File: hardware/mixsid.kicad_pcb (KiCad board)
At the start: 2 copper layers, 50.8 x 55.9 mm, 67 parts, among them P1 INPUT, P2 CONTROL, P4 SOCKET LEFT, P5 OUTPUT, P6 SOCKET RIGHT, Q1 BC547, Q2 BC547, U1 GAL16V8, U2 SID2, U3 7812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

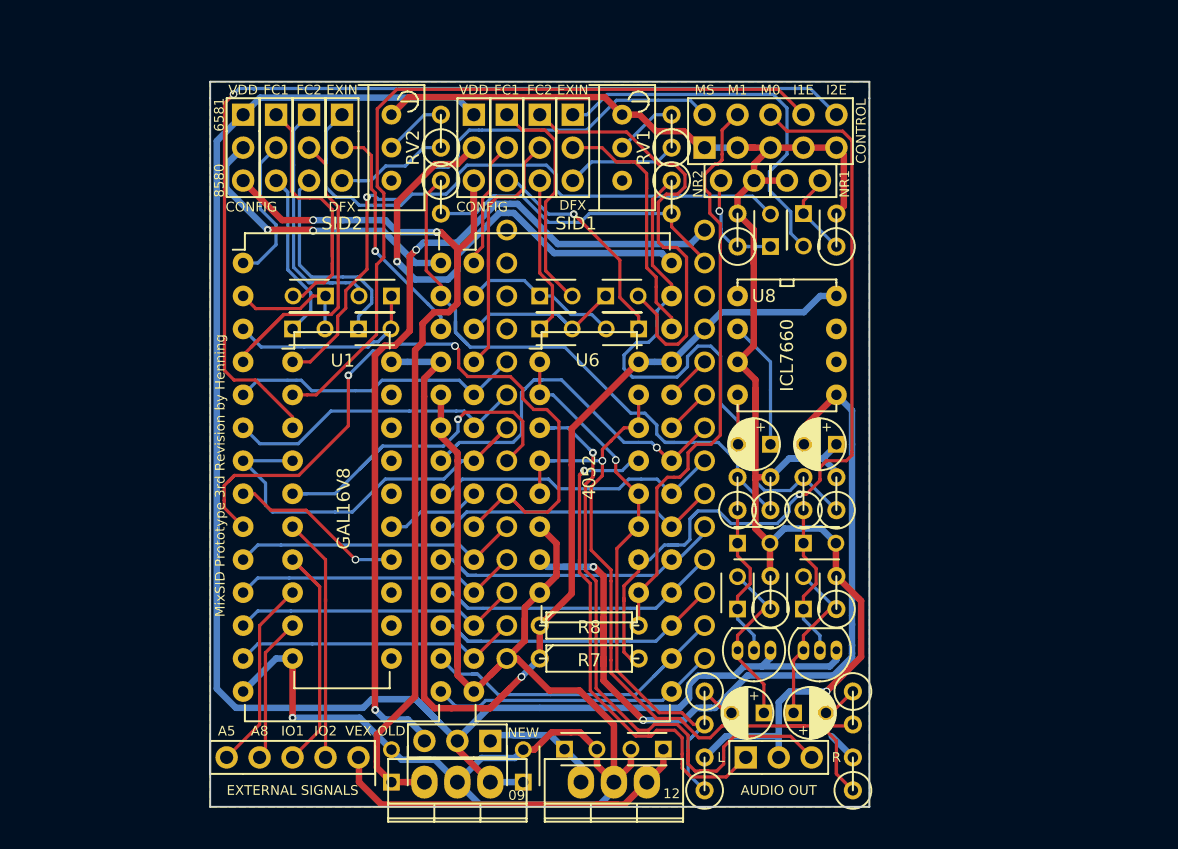
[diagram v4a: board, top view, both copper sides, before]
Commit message: Hardware: Priority, paddle multiplexing, volume adjust, bigger board size
Priority select has been reimplemented, allowing to virtually swap sids in
terms of addressing (which SID stays at home and which one goes stereo).

A 4053 multiplexer has been added to keep the paddles working regardless of
priority. Paddle lines are always routed to the SID currently at $d400.

Two pots have been added to allow volume adjustments before mixing in order
to adjust two different models in overall volume (6581 are usually louder).
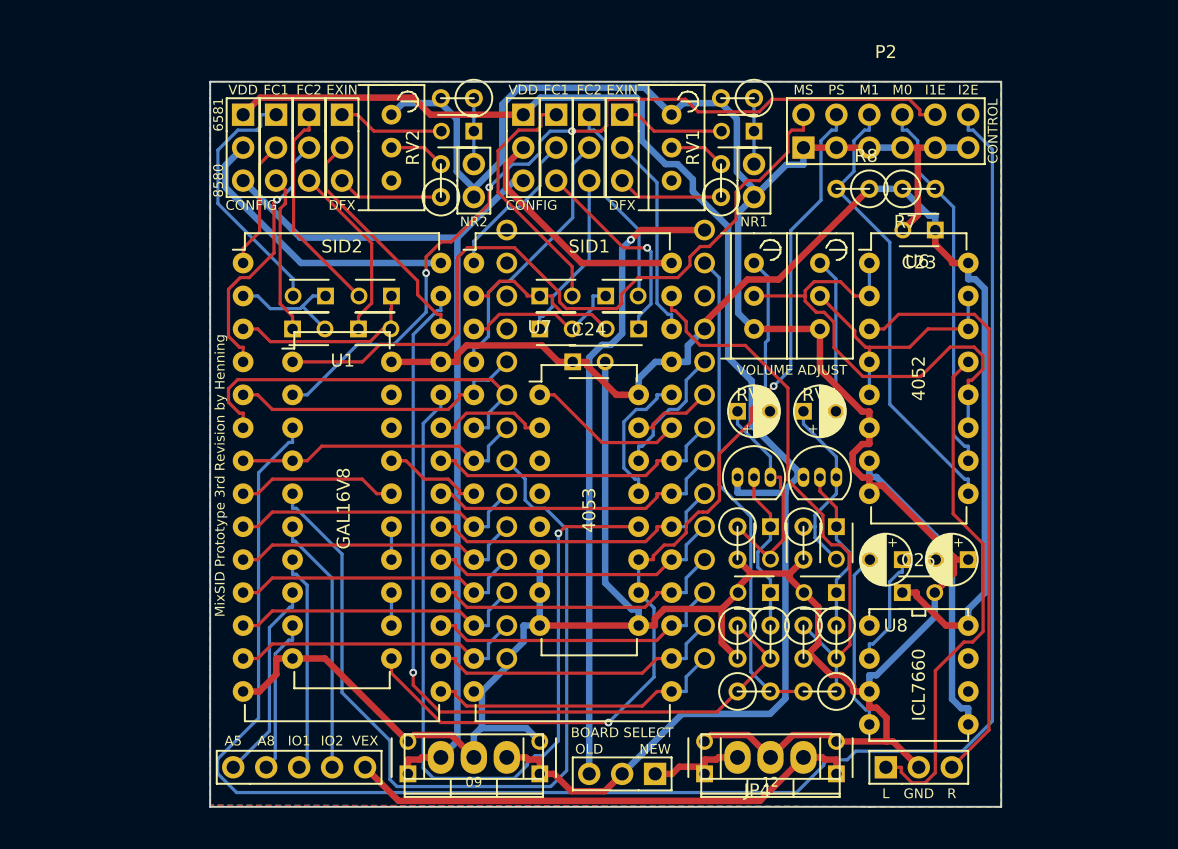
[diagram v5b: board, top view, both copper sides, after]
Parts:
- removed R15, R17: 0, Discret:R1
- removed R16, R18: ∞, Discret:R1
- added C23: 100n, Capacitors_ThroughHole:C_Disc_D3_P2.5, F.Cu at (184.2, 78.7)
- added C24: 100n, Capacitors_ThroughHole:C_Disc_D3_P2.5, F.Cu at (156.2, 88.9)
- added C25: 100n, Capacitors_ThroughHole:C_Disc_D3_P2.5, F.Cu at (181.6, 106.7)
- added RV3: 10k, Potentiometers:Potentiometer_Bourns_3296W_3-8Zoll_Inline_ScrewUp, F.Cu at (170.2, 81.3)
- added RV4: 10k, Potentiometers:Potentiometer_Bourns_3296W_3-8Zoll_Inline_ScrewUp, F.Cu at (175.3, 81.3)
- added U7: 4053, Housings_DIP:DIP-16_W7.62mm, F.Cu at (153.7, 91.4)
- P2: footprint Pinheaders:Pin_Header_Straight_2x05 -> Pinheaders:Pin_Header_Straight_2x06
- R7, R8: footprint Discret:R3 -> Discret:R1
- moved R13 45.1 mm to (170.2, 114.3), turned to 0 degrees
- moved R7 44.2 mm to (182.9, 75.6)
- moved R14 39.8 mm to (175.3, 114.3), turned to 180 degrees
- moved R8 39.3 mm to (177.8, 75.6), turned to 180 degrees
- moved U8 27.4 mm to (179.1, 109.2)
- moved U6 26.5 mm to (179.1, 81.3)
- moved C13 24.5 mm to (148.6, 71.1), turned to 180 degrees
- moved R9 23.9 mm to (147.3, 68.6), turned to 180 degrees
- moved C19 23.3 mm to (168.9, 92.7), turned to 0 degrees
- moved C22 23.3 mm to (174.0, 92.7)
- moved JP10 19.1 mm to (148.6, 73.7), turned to 0 degrees
- moved Q1 13.6 mm to (168.9, 97.8), turned to 0 degrees
- moved Q2 13.6 mm to (174.0, 97.8), turned to 0 degrees
- moved C17 13.5 mm to (181.6, 104.1)
- moved C18 13.5 mm to (186.7, 104.1)
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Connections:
- P2 pad 10: /~IO2EN -> /~IO1EN
- P2 pad 4: /M1 -> /PS
- P2 pad 6: /M0 -> /M1
- P2 pad 8: /~IO1EN -> /M0
- U1 pad 11: Net-(U1-Pad11) -> /PS
- U1 pad 13: Net-(U1-Pad13) -> Net-(U1-Pad12)
- U1 pad 14: /~CS2 -> Net-(U1-Pad14)
- U1 pad 15: /~CS1 -> Net-(U1-Pad14)
- U1 pad 16: Net-(U1-Pad16) -> /~CS2
- U1 pad 17: Net-(U1-Pad17) -> /~CS1
- U2 pad 23: GND -> /POTY2
- U2 pad 24: GND -> /POTX2
- U5 pad 23: /POTY -> /POTY1
- U5 pad 24: /POTX -> /POTX1
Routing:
- net /PS: track 0.00 -> 76.3 mm, vias 0 -> 2
- net /POTX2: track 0.00 -> 63.9 mm, vias 0 -> 1
- net /~IO2EN: track 76.7 -> 139.6 mm, vias 1 -> 0
- net /RIGHT: track 63.1 -> 20.1 mm, vias 1 -> 0
- net /VEE: track 66.3 -> 24.1 mm, vias 2 -> 0
- net Net-(C13-Pad2): track 46.3 -> 8.19 mm
- net /~CS: track 28.4 -> 66.0 mm, vias 1 -> 0
- net /M0: track 64.3 -> 29.2 mm, vias 1 -> 0
- net /A0: track 57.8 -> 23.0 mm, vias 2 -> 0
- net Net-(C14-Pad2): track 29.9 -> 8.19 mm
- net /PWR1: track 38.3 -> 18.8 mm, vias 1 -> 0
- net Net-(C9-Pad2): track 34.9 -> 15.8 mm
- net VDD: track 67.7 -> 48.9 mm, vias 2 -> 1
- net /S2OUT: track 48.1 -> 64.8 mm, vias 0 -> 1
- net /MONO_OUT: track 24.3 -> 37.7 mm
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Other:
- board size 50.8 x 55.9 mm -> 61 x 55.9 mm
- board text added: "BOARD SELECT"
- board text added: "GND"
- board text added: "PS"
- board text added: "VOLUME ADJUST"
- board text removed: "AUDIO OUT"
- board text removed: "EXTERNAL SIGNALS"

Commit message: Hardware: Replaced balance pots with round types (bourns 3339), rearranged
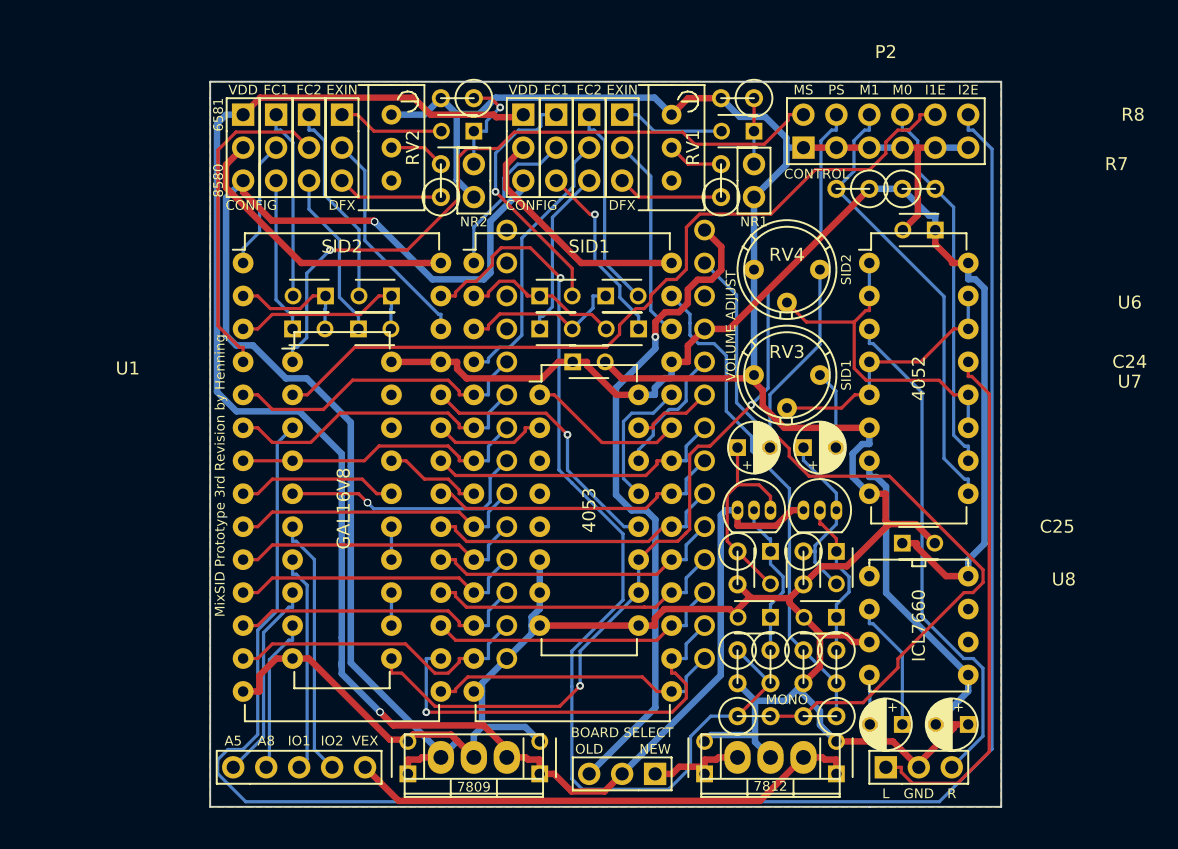
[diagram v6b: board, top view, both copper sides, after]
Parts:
- RV3, RV4: footprint Potentiometers:Potentiometer_Bourns_3296W_3-8Zoll_Inline_ScrewUp -> Potentiometers:Potentiometer_Bourns_3339P_Angular_ScrewUp
- moved C17 12.7 mm to (181.6, 116.8)
- moved C18 12.7 mm to (186.7, 116.8)
- moved RV4 8.64 mm to (175.3, 89.9)
- moved RV3 5.11 mm to (175.3, 81.8)
- moved C25 3.81 mm to (181.6, 102.9)
- moved U8 3.81 mm to (179.1, 105.4)
- moved C19 2.79 mm to (168.9, 95.5)
- moved C22 2.79 mm to (174.0, 95.5)
- moved Q1 2.54 mm to (168.9, 100.3)
- moved Q2 2.54 mm to (174.0, 100.3)
- moved C16 1.91 mm to (171.4, 103.5)
- moved C21 1.91 mm to (176.5, 103.5)
- moved R11 1.91 mm to (176.5, 112.4)
- moved R12 1.91 mm to (174.0, 104.8)
- moved R13 1.91 mm to (170.2, 116.2)
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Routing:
- net /~CS: track 66.0 -> 19.6 mm, vias 0 -> 1
- net /POTX2: track 63.9 -> 21.0 mm
- net /MONO_OUT: track 37.7 -> 58.5 mm, vias 0 -> 1
- net /+9V: track 69.5 -> 90.2 mm, vias 0 -> 1
- net GND: track 264.1 -> 243.7 mm
- net /+12V: track 115.8 -> 132.9 mm, vias 0 -> 1
- net /S2OUT: track 64.8 -> 78.6 mm
- net /LEFT: track 37.6 -> 26.7 mm
- net /D1: track 23.1 -> 33.7 mm, vias 0 -> 1
- net Net-(C17-Pad2): track 13.8 -> 3.83 mm
- net /RIGHT_OUT: track 45.1 -> 39.0 mm
- net /CLK: track 30.1 -> 24.1 mm
- net Net-(C22-Pad2): track 11.9 -> 6.10 mm
- net Net-(JP2-Pad2): track 20.2 -> 25.4 mm, vias 1 -> 0
- net Net-(C3-Pad2): track 19.8 -> 14.7 mm
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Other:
- board text added: "7809"
- board text added: "7812"
- board text added: "MONO"
- board text added: "SID1"
- board text added: "SID2"
- board text removed: "09"
- board text removed: "12"

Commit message: Firmware/Hardware: RW2 signal controls SID2 RW during parallel addressing
Depending on RW2, SID2 is write-only or read-write when addressed alongside
SID1.

The default setting is write-only to assure proper paddle support.
For mono tunes that use the readable registers for special effects,
parallel addressing would result in only one SID playing those effects
properly, thus RW2 allows the user to make both sids read-write.
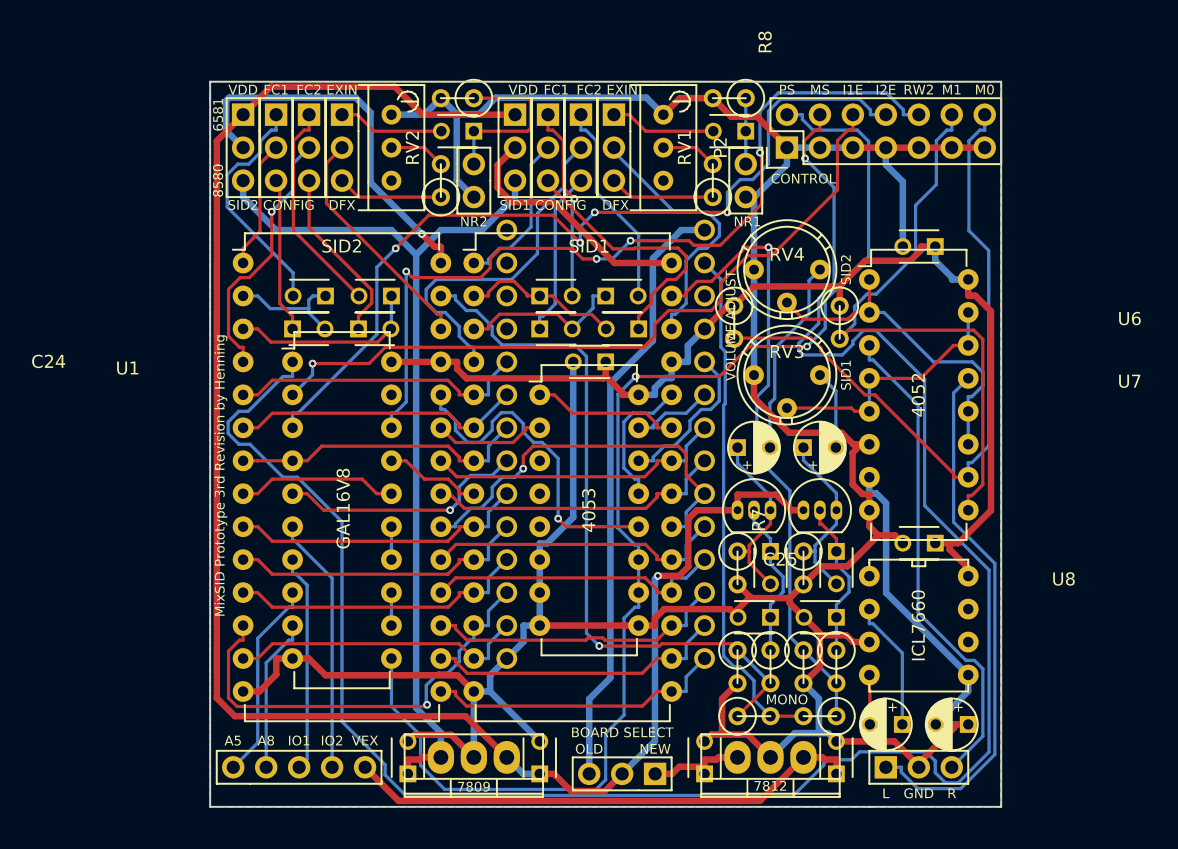
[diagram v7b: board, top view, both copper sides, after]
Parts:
- P2: footprint Pinheaders:Pin_Header_Straight_2x06 -> Pin_Headers:Pin_Header_Straight_2x07
- moved R7 17.6 mm to (168.7, 85.9), turned to 270 degrees
- moved R8 10.3 mm to (176.8, 85.9), turned to 270 degrees
- moved C24 2.54 mm to (158.8, 88.9), turned to 180 degrees
- moved C25 2.54 mm to (184.2, 102.9), turned to 180 degrees
- moved C23 1.27 mm to (184.2, 80.0)
- moved P2 1.27 mm to (172.7, 72.4)
- moved U6 1.27 mm to (179.1, 82.5)
- moved C14 0.64 mm to (169.5, 71.1)
- moved JP11 0.64 mm to (159.4, 69.8)
- moved JP5 0.64 mm to (151.8, 69.8)
- moved JP9 0.64 mm to (169.5, 73.7)
- moved RV1 0.64 mm to (163.2, 69.8)
- moved JP6 0.63 mm to (156.8, 69.8)
- moved JP7 0.63 mm to (154.3, 69.8)
- moved R10 0.63 mm to (167.0, 74.9)
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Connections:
- P2 pad 10: /~IO1EN -> /~RW2
- P2 pad 12: /~IO2EN -> /M1
- P2 pad 2: /MS -> /PS
- P2 pad 4: /PS -> /MS
- P2 pad 6: /M1 -> /~IO1EN
- P2 pad 8: /M0 -> /~IO2EN
- U1 pad 18: Net-(U1-Pad18) -> /~RW2
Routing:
- net /MS: track 53.7 -> 156.2 mm
- net /~IO2EN: track 141.8 -> 66.4 mm, vias 0 -> 4
- net /~RW2: track 0.00 -> 65.0 mm, vias 0 -> 4
- net /PS: track 71.3 -> 97.5 mm
- net /S2OUT: track 78.6 -> 54.5 mm
- net /M0: track 29.2 -> 52.9 mm
- net /+9V: track 90.2 -> 70.4 mm, vias 1 -> 0
- net /MONO_OUT: track 58.5 -> 39.9 mm, vias 1 -> 0
- net /M1: track 34.9 -> 46.9 mm
- net /A3: track 23.1 -> 34.3 mm, vias 0 -> 1
- net /D1: track 33.7 -> 23.1 mm, vias 1 -> 0
- net /S1OUT: track 38.4 -> 48.2 mm, vias 0 -> 1
- net GND: track 243.7 -> 251.5 mm
- net /PWR2: track 22.6 -> 30.0 mm, vias 0 -> 1
- net /D5: track 23.4 -> 30.8 mm, vias 0 -> 1
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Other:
- board text added: "RW2"
- board text added: "SID1 CONFIG"
- board text added: "SID2 CONFIG"
- board text removed: "CONFIG"

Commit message: Hardware: Use round pots fot digifix as well
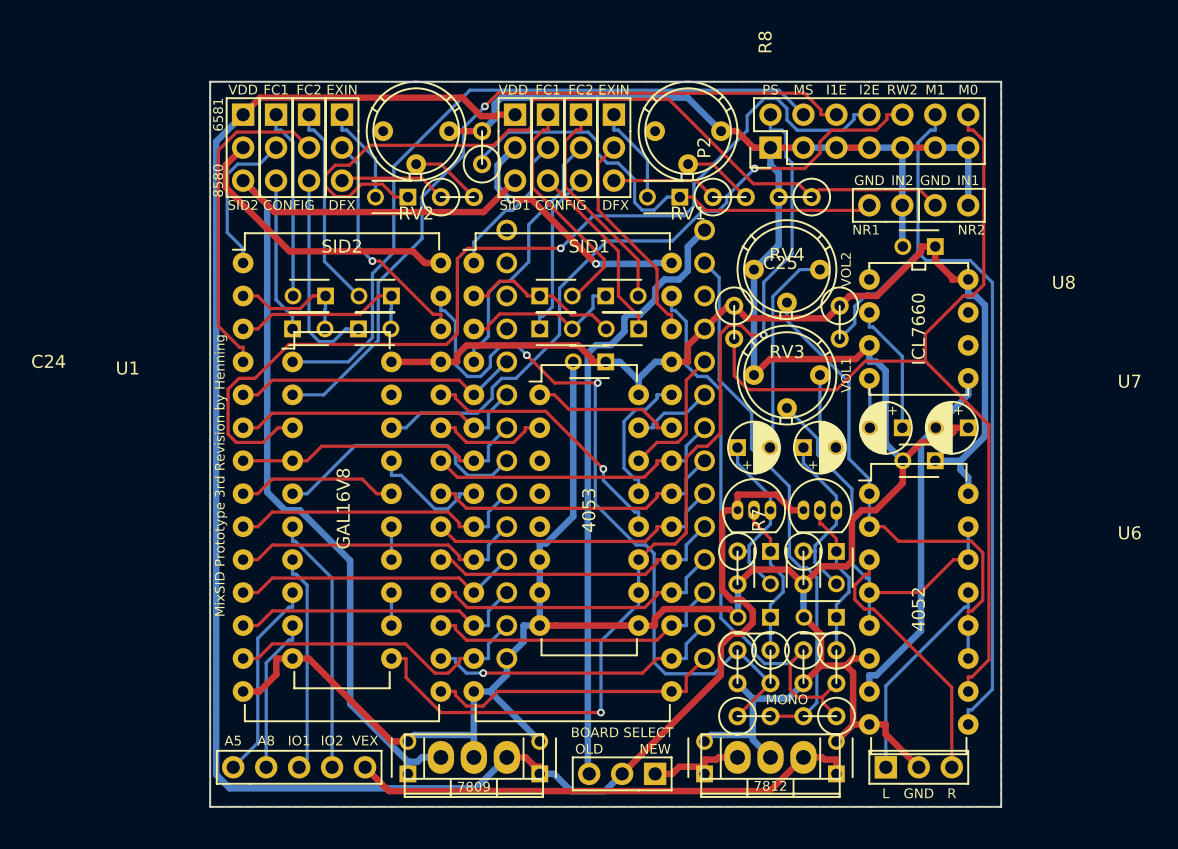
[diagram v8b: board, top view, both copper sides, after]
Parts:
- RV1, RV2: footprint Potentiometers:Potentiometer_Bourns_3296W_3-8Zoll_Inline_ScrewUp -> Potentiometers:Potentiometer_Bourns_3339P_Angular_ScrewUp
- moved JP10 35.7 mm to (184.2, 76.8), turned to 90 degrees
- moved R9 27.1 mm to (173.4, 76.2)
- moved C17 22.9 mm to (181.6, 94.0)
- moved C18 22.9 mm to (186.7, 94.0)
- moved C25 22.9 mm to (184.2, 80.0)
- moved U8 22.9 mm to (179.1, 82.5)
- moved R2 19.4 mm to (149.2, 72.4), turned to 90 degrees
- moved U6 16.5 mm to (179.1, 99.1)
- moved C23 16.5 mm to (184.2, 96.5)
- moved JP9 10.0 mm to (179.1, 76.8), turned to 90 degrees
- moved C13 7.18 mm to (143.5, 76.2)
- moved C14 7.18 mm to (164.5, 76.2)
- moved RV1 4.62 mm to (167.6, 71.1)
- moved RV2 4.62 mm to (146.7, 71.1)
- moved R10 1.80 mm to (168.3, 76.2), turned to 0 degrees
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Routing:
- net /MS: track 156.2 -> 55.6 mm, vias 1 -> 0
- net Net-(C13-Pad1): track 13.6 -> 62.7 mm
- net Net-(C14-Pad1): track 5.08 -> 36.2 mm
- net /LEFT_OUT: track 41.2 -> 16.3 mm
- net /PS: track 97.5 -> 76.3 mm
- net /RIGHT_OUT: track 37.7 -> 20.1 mm
- net /M0: track 52.9 -> 69.2 mm
- net /M1: track 46.9 -> 62.6 mm
- net /~RW2: track 65.0 -> 52.9 mm, vias 4 -> 1
- net /LEFT: track 26.5 -> 38.3 mm
- net /A3: track 34.3 -> 23.0 mm, vias 1 -> 0
- net /RIGHT: track 20.2 -> 30.7 mm
- net /~IO2EN: track 66.4 -> 75.2 mm, vias 4 -> 1
- net VCC: track 84.4 -> 75.9 mm
- net /D5: track 30.8 -> 23.1 mm, vias 1 -> 0
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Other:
- board text added: "IN1"
- board text added: "IN2"
- board text added: "VOL1"
- board text added: "VOL2"
- board text removed: "CONTROL"
- board text removed: "SID1"
- board text removed: "SID2"
- board text removed: "VOLUME ADJUST"
